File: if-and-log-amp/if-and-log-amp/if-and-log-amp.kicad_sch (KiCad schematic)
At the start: 70 parts, among them J301 Conn_Coaxial, J302 Conn_01x02_Male, J303 Conn_01x02_Male, J304 Conn_01x02_Male, J305 Conn_01x02_Male, J306 Conn_01x02_Male, J307 Board to Box Ground, SW301 Video, U301 AD603AQ, U302 L78L05_TO92, U303 LM317L_TO92, U304 AD8307AN, U305 CA3140

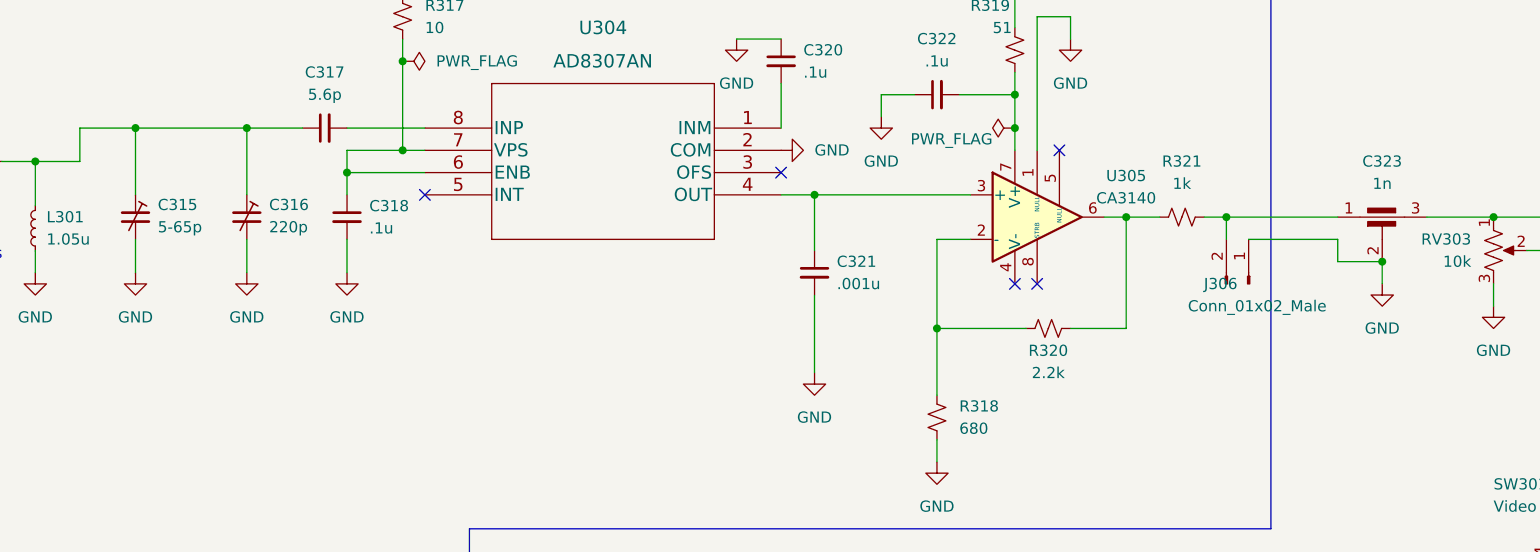
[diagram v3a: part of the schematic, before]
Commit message: updates to 15v supply and if and log amp boards so boards can be sent to fab
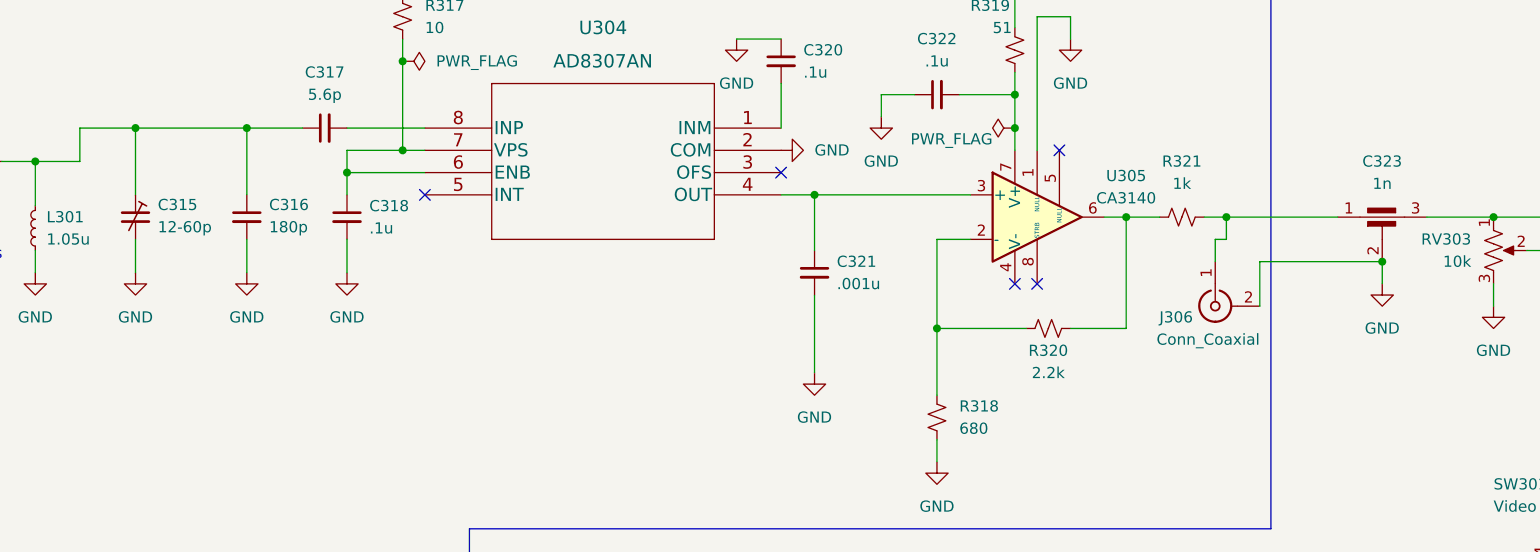
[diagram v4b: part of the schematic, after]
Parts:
- removed J306: Conn_01x02_Male, Connector_Wire:SolderWire-0.15sqmm_1x02_P4mm_D0.5mm_OD1.5mm, symbol Connector:Conn_01x02_Male
- added J306: Conn_Coaxial, if-log-amp:MOLEX_73391-0060, symbol Connector:Conn_Coaxial
- C315: value 5-65p -> 12-60p
- C316: value 220p -> 180p; symbol Device:C_Trim_Small -> Device:C_Small
- J301: footprint Connector_Wire:SolderWire-0.15sqmm_1x02_P4mm_D0.5mm_OD1.5mm -> if-log-amp:MOLEX_73391-0060
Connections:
- net GND: now also J306.2 (Ext)
- net at C323.1, R321.2: now also J306.1 (In)
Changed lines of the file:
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@@
+    (stroke (width 0) (type default) (color 0 0 0 0))
+  )
+  (wire (pts (xy 295.91 82.55) (xy 295.91 77.47))
     (stroke (width 0) (type default) (color 0 0 0 0))
   )
@@
     (stroke (width 0) (type default) (color 0 0 0 0))
   )
-  (wire (pts (xy 309.88 77.47) (xy 304.8 77.47))
-    (stroke (width 0) (type default) (color 0 0 0 0))
-  )
   (wire (pts (xy 101.6 165.1) (xy 101.6 161.29))
     (stroke (width 0) (type default) (color 0 0 0 0))
@@
     (stroke (width 0) (type default) (color 0 0 0 0))
   )
-  (wire (pts (xy 304.8 74.93) (xy 294.64 74.93))
-    (stroke (width 0) (type default) (color 0 0 0 0))
-  )
   (wire (pts (xy 43.18 151.13) (xy 43.18 154.94))
     (stroke (width 0) (type default) (color 0 0 0 0))
@@
     (stroke (width 0) (type default) (color 0 0 0 0))
   )
+  (wire (pts (xy 292.1 74.93) (xy 290.83 74.93))
+    (stroke (width 0) (type default) (color 0 0 0 0))
+  )
   (wire (pts (xy 191.77 129.54) (xy 191.77 137.16))
     (stroke (width 0) (type default) (color 0 0 0 0))
@@
     (stroke (width 0) (type default) (color 0 0 0 0))
   )
-  (wire (pts (xy 304.8 77.47) (xy 304.8 74.93))
-    (stroke (width 0) (type default) (color 0 0 0 0))
-  )
   (wire (pts (xy 58.42 52.07) (xy 58.42 49.53))
     (stroke (width 0) (type default) (color 0 0 0 0))
@@
     (stroke (width 0) (type default) (color 0 0 0 0))
   )
+  (wire (pts (xy 290.83 74.93) (xy 290.83 77.47))
+    (stroke (width 0) (type default) (color 0 0 0 0))
+  )
   (wire (pts (xy 177.8 162.56) (xy 177.8 176.53))
     (stroke (width 0) (type default) (color 0 0 0 0))
@@
   )
   (wire (pts (xy 328.93 111.76) (xy 323.85 111.76))
+    (stroke (width 0) (type default) (color 0 0 0 0))
+  )
+  (wire (pts (xy 295.91 77.47) (xy 309.88 77.47))
     (stroke (width 0) (type default) (color 0 0 0 0))
   )
@@
     )
     (pin "1")
-  )
-  (symbol (lib_id "Connector:Conn_01x02_Male") (at 294.64 80.01 270) (mirror x) (unit 1)
-    (in_bom yes) (on_board yes)
-    (property "Reference" "J306" (id 0) (at 293.37 80.01 90)
-      (effects (font (size 1.27 1.27)) (justify right))
-    )
-    (property "Value" "Conn_01x02_Male" (id 1) (at 303.53 82.55 90)
-      (effects (font (size 1.27 1.27)) (justify right))
-    )
-    (property "Footprint" "Connector_Wire:SolderWire-0.15sqmm_1x02_P4mm_D0.5mm_OD1.5mm" (id 2) (at 294.64 80.01 0)
-      (effects (font (size 1.27 1.27)) hide)
-    )
-    (property "Datasheet" "~" (id 3) (at 294.64 80.01 0)
-      (effects (font (size 1.27 1.27)) hide)
-    )
-    (pin "1")
-    (pin "2")
   )
   (symbol (lib_id "Device:R_Potentiometer_US") (at 165.1 170.18 0) (unit 1)
@@
     (pin "1")
   )
+  (symbol (lib_id "Connector:Conn_Coaxial") (at 290.83 82.55 90) (mirror x) (unit 1)
+    (in_bom yes) (on_board yes)
+    (property "Reference" "J306" (id 0) (at 288.29 83.82 90)
+      (effects (font (size 1.27 1.27)) (justify left))
+    )
+    (property "Value" "Conn_Coaxial" (id 1) (at 295.91 86.36 90)
+      (effects (font (size 1.27 1.27)) (justify left))
+    )
+    (property "Footprint" "if-log-amp:MOLEX_73391-0060" (id 2) (at 290.83 82.55 0)
+      (effects (font (size 1.27 1.27)) hide)
+    )
+    (property "Datasheet" "https://www.molex.com/pdm_docs/ps/PS-89675-346.pdf" (id 3) (at 290.83 82.55 0)
+      (effects (font (size 1.27 1.27)) hide)
+    )
+    (property "Spice_Primitive" "J" (id 4) (at 290.83 82.55 0)
+      (effects (font (size 1.27 1.27)) hide)
+    )
+    (property "Spice_Model" "Conn_Coaxial" (id 5) (at 290.83 82.55 0)
+      (effects (font (size 1.27 1.27)) hide)
+    )
+    (property "Spice_Netlist_Enabled" "N" (id 6) (at 290.83 82.55 0)
+      (effects (font (size 1.27 1.27)) hide)
+    )
+    (pin "1")
+    (pin "2")
+  )
   (symbol (lib_id "Device:R_Small_US") (at 128.27 151.13 0) (unit 1)
     (in_bom yes) (on_board yes) (fields_autoplaced)
@@
     (property "Reference" "J301" (id 0) (at 39.6874 60.96 0))
     (property "Value" "Conn_Coaxial" (id 1) (at 39.6874 63.5 0))
-    (property "Footprint" "Connector_Wire:SolderWire-0.15sqmm_1x02_P4mm_D0.5mm_OD1.5mm" (id 2) (at 39.37 68.58 0)
-      (effects (font (size 1.27 1.27)) hide)
-    )
-    (property "Datasheet" " ~" (id 3) (at 39.37 68.58 0)
+    (property "Footprint" "if-log-amp:MOLEX_73391-0060" (id 2) (at 39.37 68.58 0)
+      (effects (font (size 1.27 1.27)) hide)
+    )
+    (property "Datasheet" "https://www.molex.com/pdm_docs/ps/PS-89675-346.pdf" (id 3) (at 39.37 68.58 0)
       (effects (font (size 1.27 1.27)) hide)
     )
@@
       (effects (font (size 1.27 1.27)) (justify left))
     )
-    (property "Value" "5-65p" (id 1) (at 170.18 73.5329 0)
+    (property "Value" "12-60p" (id 1) (at 170.18 73.5329 0)
       (effects (font (size 1.27 1.27)) (justify left))
     )
@@
     (pin "2")
   )
-  (symbol (lib_id "Device:C_Trim_Small") (at 180.34 72.39 0) (unit 1)
+  (symbol (lib_id "Device:C_Small") (at 180.34 72.39 0) (unit 1)
     (in_bom yes) (on_board yes) (fields_autoplaced)
     (property "Reference" "C316" (id 0) (at 182.88 70.9929 0)
       (effects (font (size 1.27 1.27)) (justify left))
     )
-    (property "Value" "220p" (id 1) (at 182.88 73.5329 0)
+    (property "Value" "180p" (id 1) (at 182.88 73.5329 0)
       (effects (font (size 1.27 1.27)) (justify left))
     )
@@
     )
     (path "/6da294e0-d0ea-4520-9eae-214e4e104da5"
-      (reference "C315") (unit 1) (value "5-65p") (footprint "if-log-amp:GKG60015")
+      (reference "C315") (unit 1) (value "12-60p") (footprint "if-log-amp:GKG60015")
     )
     (path "/aa7337a7-5d79-4c08-a459-a9e6ac935626"
-      (reference "C316") (unit 1) (value "220p") (footprint "Capacitor_THT:C_Radial_D4.0mm_H5.0mm_P1.50mm")
+      (reference "C316") (unit 1) (value "180p") (footprint "Capacitor_THT:C_Radial_D4.0mm_H5.0mm_P1.50mm")
     )
     (path "/78209a31-876f-4c56-841c-74e6cb8fd1d6"
@@
     )
     (path "/6987431d-46da-4786-8718-591cfd165b0a"
-      (reference "J301") (unit 1) (value "Conn_Coaxial") (footprint "Connector_Wire:SolderWire-0.15sqmm_1x02_P4mm_D0.5mm_OD1.5mm")
+      (reference "J301") (unit 1) (value "Conn_Coaxial") (footprint "if-log-amp:MOLEX_73391-0060")
     )
     (path "/330bea58-49da-44f4-afd5-32451222966b"
@@
       (reference "J305") (unit 1) (value "Conn_01x02_Male") (footprint "Connector_Wire:SolderWire-0.15sqmm_1x02_P4mm_D0.5mm_OD1.5mm")
     )
-    (path "/097c41bc-eb3d-4c20-a9c7-7d2f15dbb60f"
-      (reference "J306") (unit 1) (value "Conn_01x02_Male") (footprint "Connector_Wire:SolderWire-0.15sqmm_1x02_P4mm_D0.5mm_OD1.5mm")
+    (path "/26c102a2-099b-461f-b2e9-557069d75d96"
+      (reference "J306") (unit 1) (value "Conn_Coaxial") (footprint "if-log-amp:MOLEX_73391-0060")
     )
     (path "/077ce07b-7c94-4f61-8ba0-b534b0cdfb33"

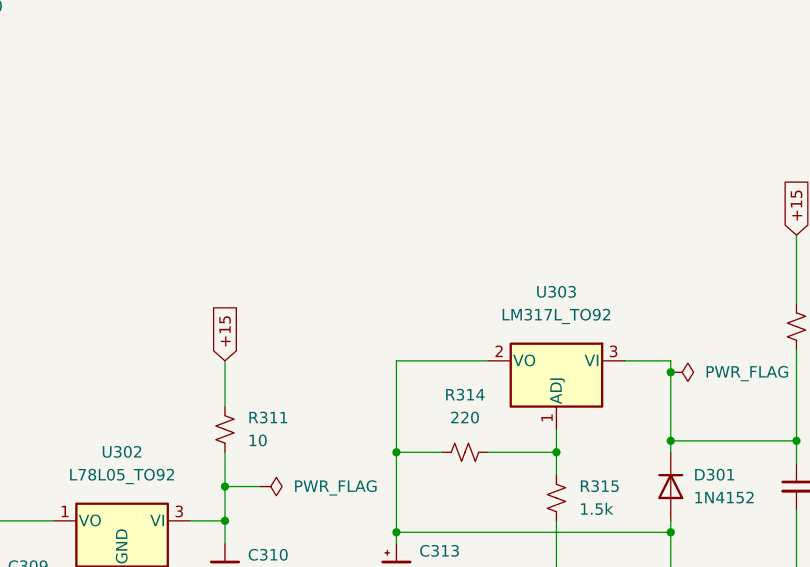
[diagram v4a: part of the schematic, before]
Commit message: some improvements to timebase and if log amp
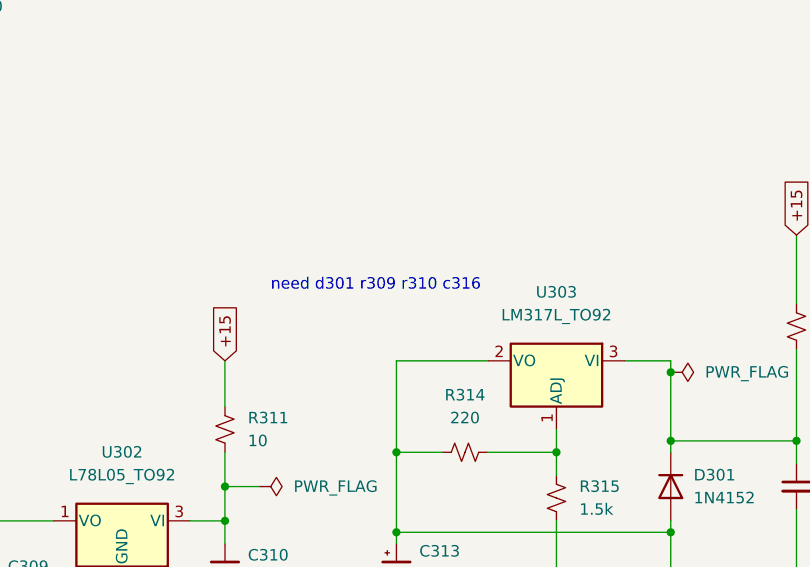
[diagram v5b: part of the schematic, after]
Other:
- note added: "need d301 r309 r310 c316"
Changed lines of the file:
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@@
   (title_block
     (title "Spectrum Analyzer IF and Log Amp")
-    (date "2022-06-12")
-    (rev "0.0")
+    (date "2022-07-18")
+    (rev "1.0")
     (company "Andy McCann KA3KAF and Doug McCann KA3KAG")
     (comment 2 "Wes Hayward W7ZOI")
@@
     (effects (font (size 1.27 1.27)) (justify left bottom))
   )
+  (text "need d301 r309 r310 c316" (at 133.35 135.89 0)
+    (effects (font (size 1.27 1.27)) (justify left bottom))
+  )

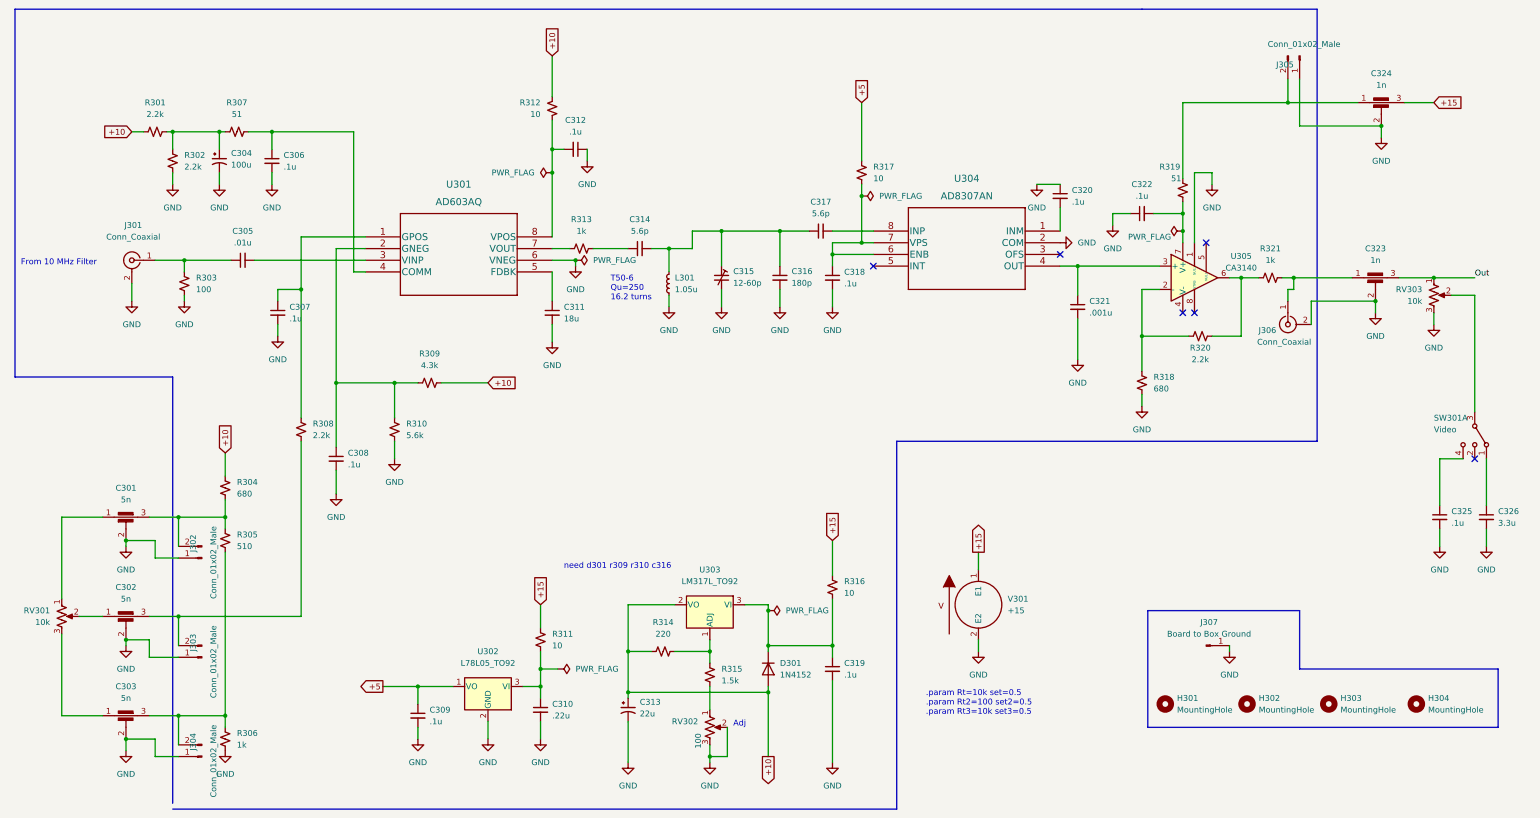
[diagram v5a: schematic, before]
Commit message: Rev 1 Changes for if and log amp
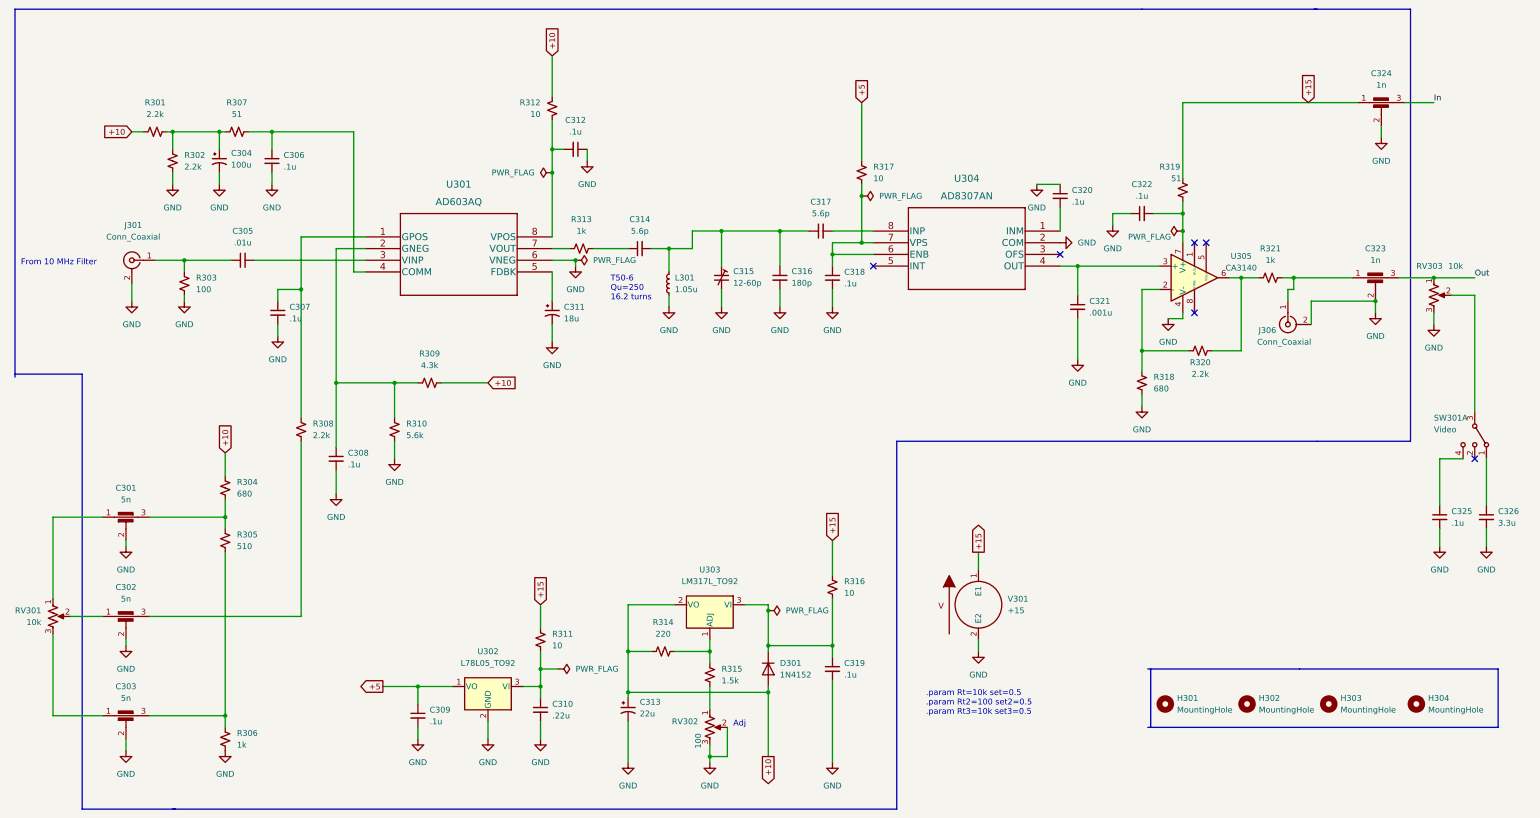
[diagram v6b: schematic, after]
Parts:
- removed J302, J303, J304, J305: Conn_01x02_Male, Connector_Wire:SolderWire-0.15sqmm_1x02_P4mm_D0.5mm_OD1.5mm, symbol Connector:Conn_01x02_Male
- removed J307: Board to Box Ground, Connector_Wire:SolderWire-0.15sqmm_1x01_D0.5mm_OD1.5mm, symbol Connector:Conn_01x01_Male
- C301, C302, C303, C323, C324: footprint (none) -> if-log-amp:DSS1NB32A102Q91A
- C311: symbol Device:C_Small -> Device:C_Polarized_Small_US
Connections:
- net +15: now also C324.1, R319.2; no longer C324.3
- net GND: now also U305.4 (V-); no longer U305.1 (NULL)
- new net In: C324.3
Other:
- note removed: "need d301 r309 r310 c316"
- moved on the sheet: R320, RV301
